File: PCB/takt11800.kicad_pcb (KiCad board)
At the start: 2 copper layers, 391.2 x 166.5 mm, 284 parts, among them J1 SWD Interface, J3 USB_C, J4 Conn_01x05_Pin, SW1 BOOT, SW2 NRST, U1 STM32F072CBT6, U2 CD74HC4067SM, U3 XC6206, U4 USBLC6-2SC6

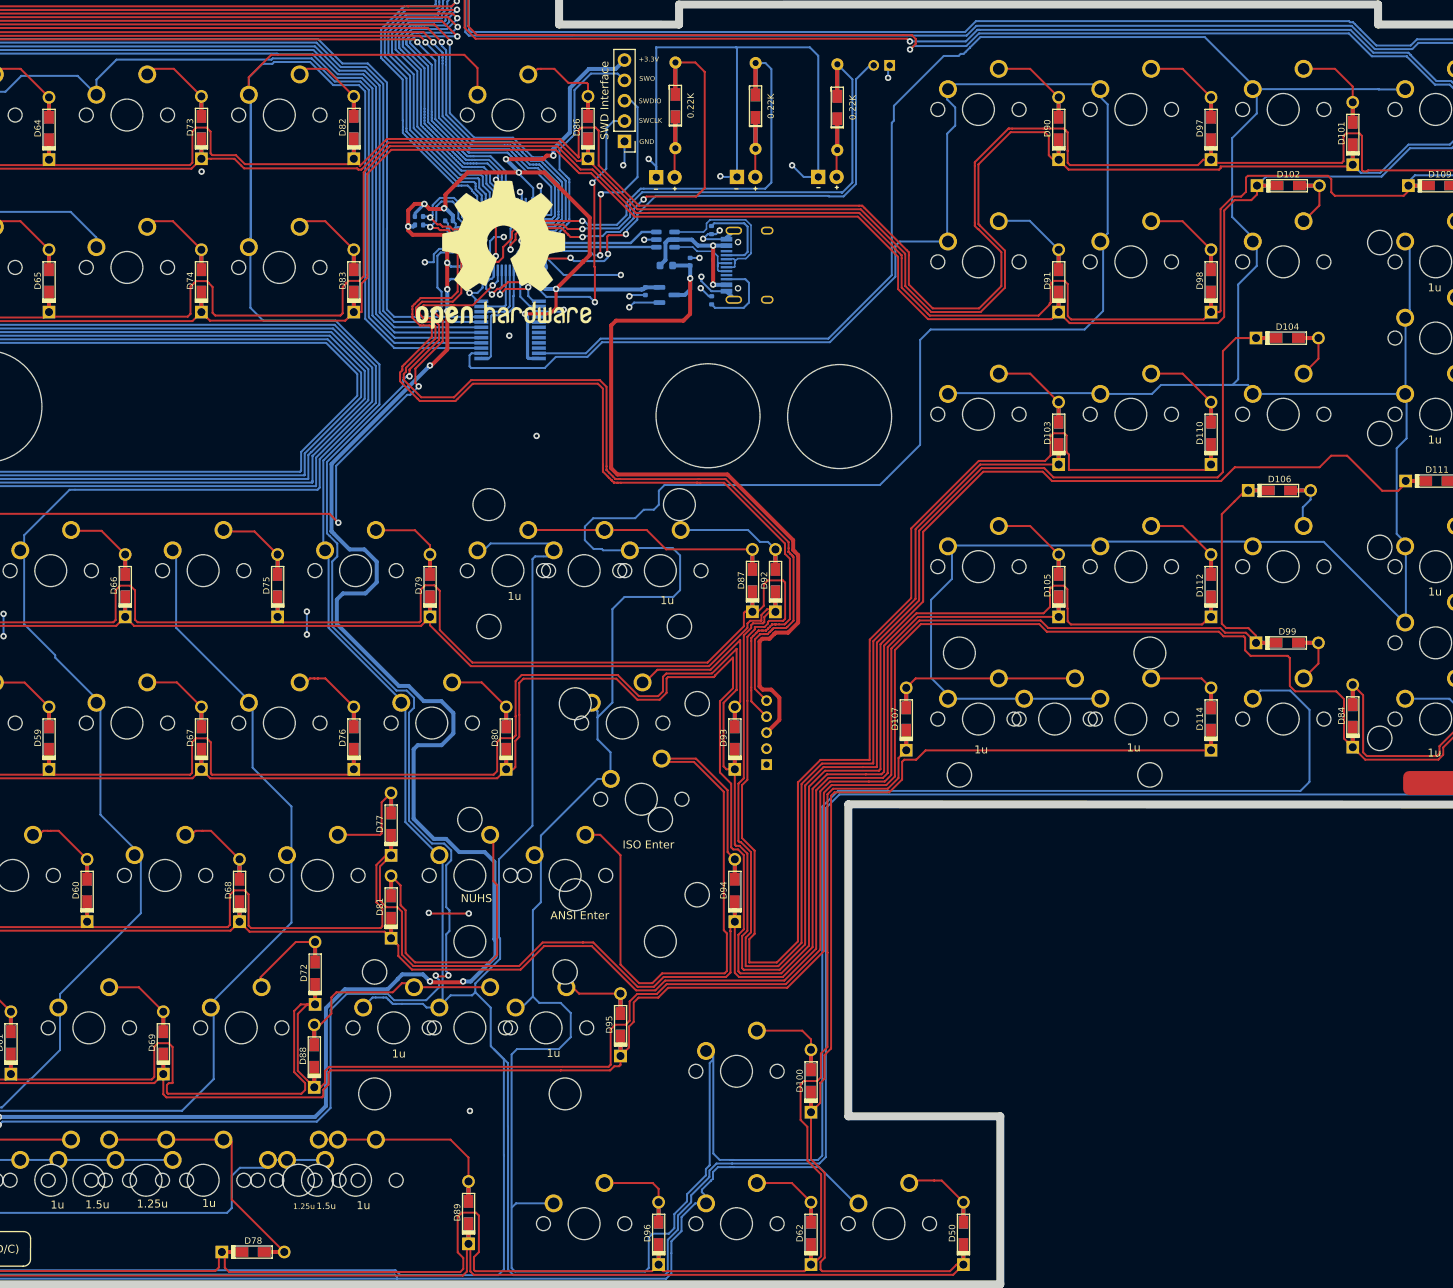
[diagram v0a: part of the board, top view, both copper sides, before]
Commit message: update USB-C footprint; adjust arrow keys position; cleanup libraries
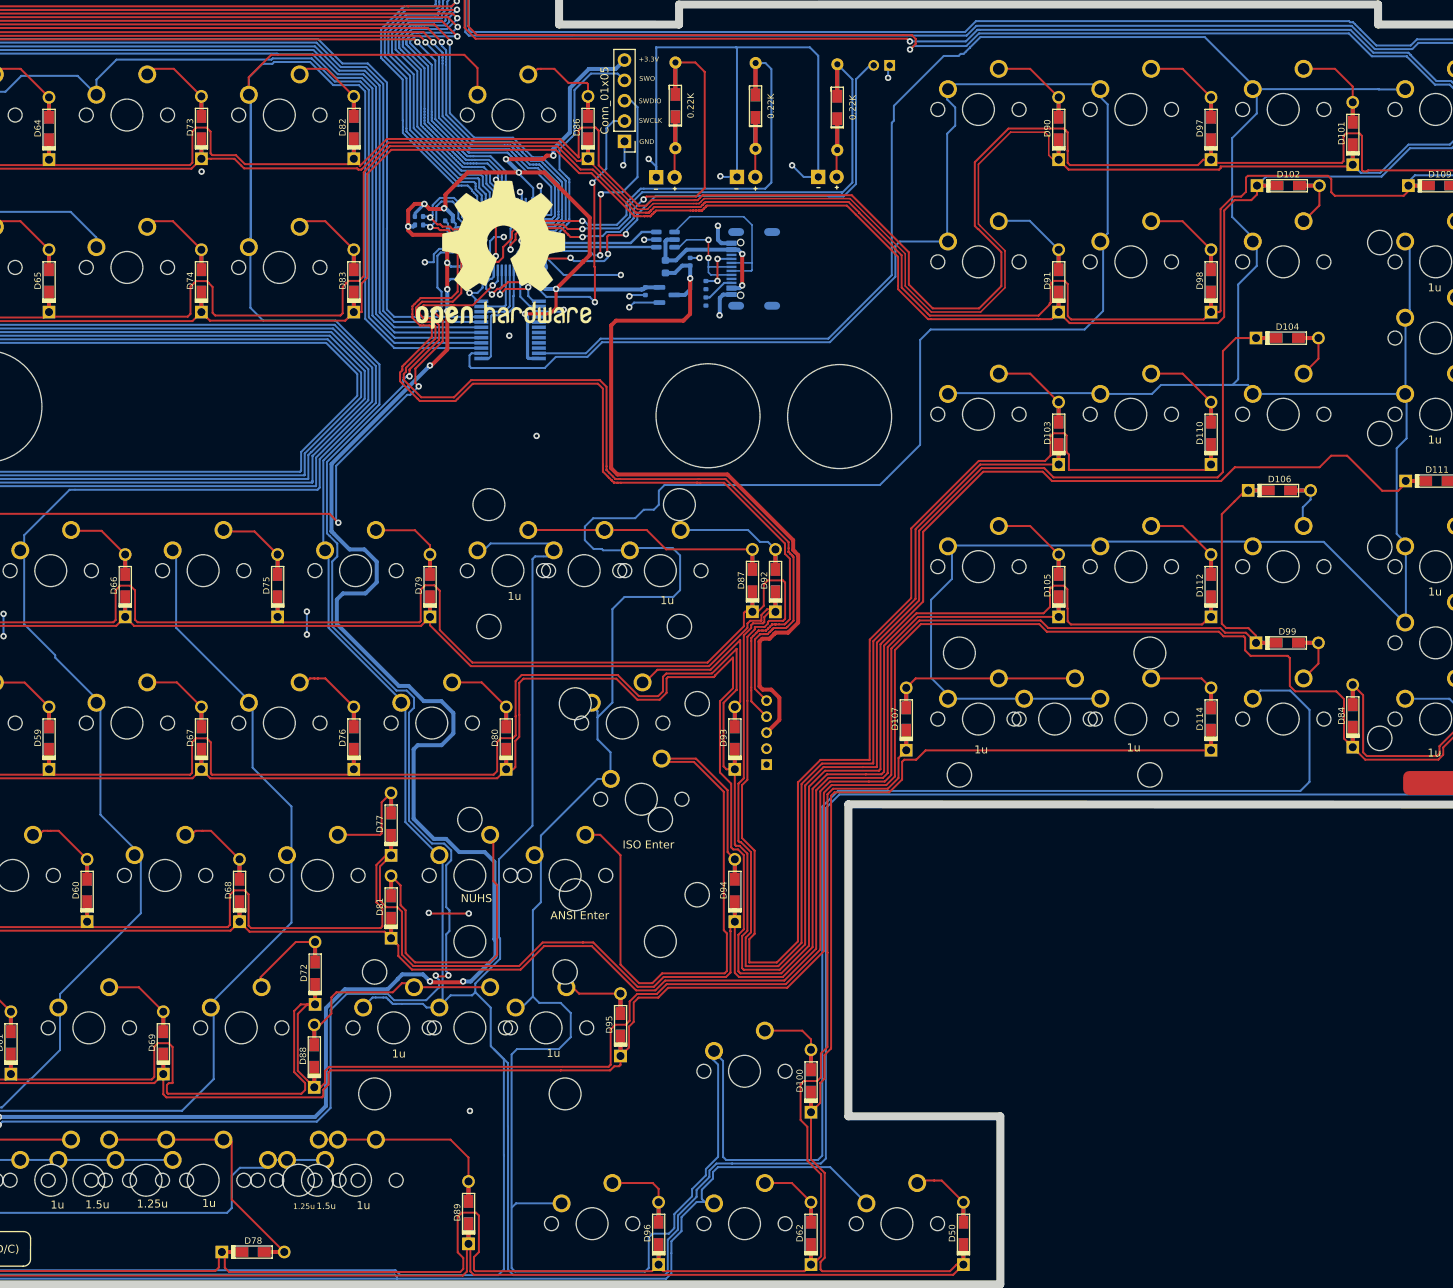
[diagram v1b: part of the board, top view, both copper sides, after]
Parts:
- removed J3: USB_C, ScottoKeebs_Components:USB_C_HRO_TYPE-C-31-M-12
- added J2: USB4800-03-A, footprints:CONN_USB4800_GCT, B.Cu at (308.4, 99.0)
- F1: footprint ScottoKeebs_Components:Fuse_0603 -> footprints:Fuse_0603
- J1: value SWD Interface -> Conn_01x05
- moved R7 6.91 mm to (301.2, 101.0)
- moved arrow-down-key1 1.00 mm to (306.0, 218.3)
- moved arrow-left-key1 1.00 mm to (287.0, 218.3)
- moved arrow-right-key1 1.00 mm to (325.1, 218.3)
- moved arrow-up-key1 1.00 mm to (306.0, 199.3)
- moved R8 0.73 mm to (301.2, 103.1)
- moved F1 0.18 mm to (296.1, 98.7), turned to -90 degrees
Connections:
- R8 pad 1: Net-(J3-CC2) -> GND
- R8 pad 2: GND -> Net-(J2-CC2)
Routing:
- net Net-(J3-CC2): track 10.6 -> 0.00 mm
- net GND: track 188.4 -> 181.3 mm, vias 43 -> 41
- net Net-(J2-CC1): track 10.8 -> 6.10 mm, vias 0 -> 2
- net /USB_D+: track 10.3 -> 14.6 mm, vias 0 -> 2
- net Net-(J2-CC2): track 0.00 -> 3.95 mm
- net col4: track 723.9 -> 725.9 mm
- net VBUS: track 17.8 -> 19.4 mm
- net /USB_D-: track 20.1 -> 21.7 mm
- net +5V: track 96.8 -> 98.0 mm
- net row2: track 594.7 -> 595.8 mm
- net row3: track 553.2 -> 554.3 mm
- net row1: track 551.0 -> 552.1 mm
- net row0: track 649.5 -> 650.5 mm
